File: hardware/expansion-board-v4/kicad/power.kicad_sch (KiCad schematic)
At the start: 37 parts, among them J9 MX1.25WT-2P BAT, U1 ME6211C33M5, U18 CH224K, U19 SY6970, U2 TPS7A2033PDBVR, U20 SY7069, U3 TPS7A2033PDBVR

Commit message: fix(hw): 103AT-2 是插件不是贴片，封装/焊盘/位置全部修正
## 主 bug：RT1 用错封装

103AT-2（SEMITEC 日本石塚）是**轴向引线玻璃封装的插件**，我之前直接套了
R_0603_1608Metric——焊盘、3D、装配全错，根因是没查 datasheet。

改为自建 NTC_103AT-2_Leaded_P2.54mm：两个 ⌀0.7 通孔、间距 2.54mm，
courtyard 只覆盖焊盘不含本体——因为 NTC 玻璃头不留在板面，靠引线延伸
平贴到电池表面。

位置从 (136.93,87.93) 改到 **(125.5,89.5)**，两个判据：
  · CHG_NTC 到分压电阻 R39/R40 只有 4.06mm。这是高阻模拟节点，
    原位置离分压网络 30mm，长走线会耦合开关噪声
  · 焊盘落在电池投影区内，玻璃头平贴板面与电池之间（电池仓净高 11.0
    − 电池 9.5 = 1.5mm 余量，刚好容下 ⌀1.5mm 玻璃头），热耦合最好

选点时扫描了两面 courtyard（通孔件会穿透）、螺丝孔让位圈、天线禁铺区。

## 连带修复：.kicad_mod 不能写 ';;' 注释

上一轮给 MX1.25WT-2P 封装加 3D 说明时用了 ';;'，那是 Lisp 语法，
KiCad 的 S-expression 解析器不认——**整个封装文件直接加载失败**，
而且不报错，只是 FootprintLoad 返回 None。逐个测试库中封装才发现
MX1.25WT-2P 和新建的 NTC 两个都是坏的。注释一律移进 (descr ...)。

## Python 环境：按 CLAUDE.md 用 ServBay

之前 gen_bom_smt.py 报缺 openpyxl，是因为我用了 KiCad 内置的 Python
（那个只该用于需要 pcbnew 的脚本）。ServBay 的 python3 3.13.12 本来就有
openpyxl 3.1.5。现在分工明确：
  · 需要 pcbnew 的（gen_assembly/gen_checklist）→ KiCad Python
  · 纯数据处理的（gen_bom/gen_bom_smt）→ ServBay Python

BOM_采购清单.xlsx（55 项）与 BOM_嘉立创SMT.xlsx（79 料号/162 贴片位）已补出。

## 新增待决项 D3：电源区电容建议 0603 → 0805

不是为了散热（电阻功率算过，R43 最大也才 32.5mW，0603 有 3 倍余量），
而是 DC bias 衰减和耐压可得性：**C72 要 6.8µF/25V，0603 根本买不到**
（0603 在 25V 档容值上限约 1~2.2µF），而它接 9V 侧耐压不能降。
换封装会动 B 面布局，等确认。

验收：原理图↔PCB 封装零不一致，DRC error 0 条，覆铜已重填。
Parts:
- RT1: footprint Resistor_SMD:R_0603_1608Metric -> expansion-board-v4:NTC_103AT-2_Leaded_P2.54mm
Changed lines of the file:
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@@
 			(effects (font (size 1.27 1.27)))
 		)
-		(property "Footprint" "Resistor_SMD:R_0603_1608Metric"
+		(property "Footprint" "expansion-board-v4:NTC_103AT-2_Leaded_P2.54mm"
 			(at 177.8 208.28 0)
 			(effects (font (size 1.27 1.27))

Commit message: fix(hw): NTC 改用贴片 NCP18XH103F03RB —— 电池是 3M 胶贴死的，插件放不下
## 为什么又改一次

上一轮把 RT1 从 R0603 改成插件封装，理由是「103AT-2 是轴向引线玻璃件」。
那步是对的，但方案错了：**电池用 3M 胶直接贴在 B 面**（防晃动脱落，同时给
背壳散热孔留空间），板面与电池之间**没有间隙**，玻璃头无处安放。
我上一版假设有 1.5mm 余量（11.0 电池仓 − 9.5 电池），那是"电池悬空"的算法，
与实际装配方式不符。

回到贴片，但换成真正的贴片 NTC 型号，不是拿普通电阻封装凑数：
NCP18XH103F03RB（Murata 0603 10k 1%）/ TDK NTCG163JF103FT1 / 国产 0603 10K 1%。

## NTC 本身不能删

SY6970 的 TS 是锂电池充电安全强制项：<0°C 充电析锂（枝晶刺穿隔膜、内短路），
>60°C 加速老化乃至热失控。不接就得用固定电阻假装永远 25°C，等于关掉保护。

座舱 80°C 的担心已查证：TS 保护**只作用于充电路径**。高温时停充，但
PMID→SYS 直供与 BAT→SYS 放电都不受限，设备照常运行，降温自动恢复。
去掉 NTC 才会在 80°C 继续充电，那才是不可预测的后果。

## B 值差异不需要改硬件

103AT-2 是 B25/85=3435K；Murata NCP18XH103 常标 B25/50=3380K，
但同一颗料在 B25/85 口径下是 3428K——差 0.2%，保护阈值偏移 <1°C，
分压电阻 R39/R40 保持不变。要抠精度改 MCU 侧查表/Steinhart-Hart 的 B 参数。

## 位置 (125.25, 88.00)

三个约束一起解出来的：在电池投影区内直接贴电池 / 距板上开关电源 ≥19mm
（否则测的是板温不是电池温）/ CHG_NTC 到分压电阻 R39/R40 仅 4.00mm
（高阻模拟节点，走线长了耦合开关噪声）。

已删除废弃的 NTC_103AT-2_Leaded_P2.54mm 封装，免得下次误用。

验收：DRC error 0 条，原理图↔PCB 一致，全套 BOM/装配文档重生成
（BOM 88 料号、SMT 79 料号 162 贴片位、ASSEMBLY 162 件、CHECKLIST 174 位号）。
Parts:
- RT1: value 103AT-2 10k NTC -> NCP18XH103F03RB 10k NTC; footprint expansion-board-v4:NTC_103AT-2_Leaded_P2.54mm -> Resistor_SMD:R_0603_1608Metric
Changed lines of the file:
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@@
 			(effects (font (size 1.27 1.27)))
 		)
-		(property "Value" "103AT-2 10k NTC"
+		(property "Value" "NCP18XH103F03RB 10k NTC"
 			(at 177.8 205.74 0)
 			(effects (font (size 1.27 1.27)))
 		)
-		(property "Footprint" "expansion-board-v4:NTC_103AT-2_Leaded_P2.54mm"
+		(property "Footprint" "Resistor_SMD:R_0603_1608Metric"
 			(at 177.8 208.28 0)
 			(effects (font (size 1.27 1.27))

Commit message: feat(hw): 实现「单面可用」——J4 移 F 面、补 CC 下拉、电源电容改封装
## 单面可用是保底

不带电源版的 B 面现在**零贴装件**，可以走嘉立创经济型单面（¥267.1），
不必被迫上标准型双面（¥614.96）。上一版把 J4 留在 B 面，等于不带电源版
还是双面，只省 ¥35，白做。

三个改动：

  J4 (USB-C) → F 面 (144.63,73.00) rot=0
      courtyard 右沿贴齐板边 150，开口仍朝 +X（与微雪 H1 同侧）。
      翻面会镜像 x 且 USB-C 封装原点不在几何中心，x 是重新解出来的。
      USB_DP/DM 连的 R9/R10 本来就在 F 面 x117，搬过去走线反而更短；
      USB_CC1/2 与 USB_VBUS 只有带电源版才用，跨面过孔即可。

  新增 R7/R8（5.1k CC 下拉）→ F 面，紧邻 J4 2.2mm
      不带电源版没有 CH224K，CC 悬空则主机根本不认设备——USB-C 规范要求
      device 端呈现 Rd 才会被检测和枚举，不枚举就没法 UF2 刷机。
      **与 CH224K 二选一**，带电源版不贴。

  R37 (138.80,69.84) → (137.75,70.75)
      J4 的通孔安装脚穿到 B 面，落进了 R37 的 courtyard（DRC 报
      pth_inside_courtyard）。顺带把它到 CH224K CFG1 脚的距离 2.97→2.56mm。

## 电源电容改封装

不是为散热——电阻功率算过，最大的 R43 也才 (9−3.3)²/1k = 32.5mW，
0603 有 3 倍余量。真正的理由是两条：

  C72  6.8µF/25V  0603 → 1206
      接 PD 诱骗后的 9V 侧，耐压不能降。而 0603 在 25V 档容值上限只有
      1~2.2µF，6.8µF/25V 根本买不到。换封装后原位撞 C80，已就近重贴
      （按「离同网芯片引脚最近」而不是「离原位最近」找的位）。

  C73/C74/C75  10µF  0603 → 0805
      直流偏置下的容值衰减：10µF/16V X5R 在 5V 偏压下，0603 只剩
      3~4µF(−60%)，0805 还有 6~7µF(−30%)，直接影响输出纹波。

## 新增电源采购 CSV（单独一份，不混进整板 xlsx）

tools/gen_power_csv.py → BOM_电源采购_淘宝.csv，22 种料 / 30 颗。
按「卖家怎么找货」分组，同规格合并给总数，备注写清耐压/精度/为什么
封装不能换，末尾附两个版本的贴装差异。整板 88 料号的 xlsx 发给卖家太乱。

验收：DRC error 0 条，F 面丝印全通过，原理图↔PCB 零不一致，
176 元件已固化，全套文档重生成（BOM 88 料号 / SMT 79 料号 164 贴片位）。
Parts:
- C72: footprint Capacitor_SMD:C_0603_1608Metric -> Capacitor_SMD:C_1206_3216Metric
- C73, C74, C75: footprint Capacitor_SMD:C_0603_1608Metric -> Capacitor_SMD:C_0805_2012Metric
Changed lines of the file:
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@@
 			(effects (font (size 1.27 1.27)))
 		)
-		(property "Footprint" "Capacitor_SMD:C_0603_1608Metric"
+		(property "Footprint" "Capacitor_SMD:C_1206_3216Metric"
 			(at 177.8 144.78 0)
 			(effects (font (size 1.27 1.27))
@@
 			(effects (font (size 1.27 1.27)))
 		)
-		(property "Footprint" "Capacitor_SMD:C_0603_1608Metric"
+		(property "Footprint" "Capacitor_SMD:C_0805_2012Metric"
 			(at 203.2 182.88 0)
 			(effects (font (size 1.27 1.27))
@@
 			(effects (font (size 1.27 1.27)))
 		)
-		(property "Footprint" "Capacitor_SMD:C_0603_1608Metric"
+		(property "Footprint" "Capacitor_SMD:C_0805_2012Metric"
 			(at 215.9 182.88 0)
 			(effects (font (size 1.27 1.27))
@@
 			(effects (font (size 1.27 1.27)))
 		)
-		(property "Footprint" "Capacitor_SMD:C_0603_1608Metric"
+		(property "Footprint" "Capacitor_SMD:C_0805_2012Metric"
 			(at 203.2 195.58 0)
 			(effects (font (size 1.27 1.27))

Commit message: fix(v4): correct RF and power networks for V4.2
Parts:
- C72: value 6.8uF -> 10uF
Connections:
- net USB_CC1: now also U18.7 (CC2); no longer U18.6 (CC1)
- net USB_CC2: now also U18.6 (CC1); no longer U18.7 (CC2)
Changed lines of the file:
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@@
+		(effects (font (size 1.27 1.27)) (justify left))
+	)
+	(global_label "USB_CC2"
+		(shape passive)
+		(at 93.98 162.56 0)
 		(effects (font (size 1.27 1.27)) (justify left))
 	)
 	(global_label "USB_CC1"
-		(shape passive)
-		(at 93.98 162.56 0)
-		(effects (font (size 1.27 1.27)) (justify left))
-	)
-	(global_label "USB_CC2"
 		(shape passive)
 		(at 93.98 165.1 0)
@@
 			(effects (font (size 1.27 1.27)))
 		)
-		(property "Value" "6.8uF"
+		(property "Value" "10uF"
 			(at 177.8 142.24 0)
 			(effects (font (size 1.27 1.27)))

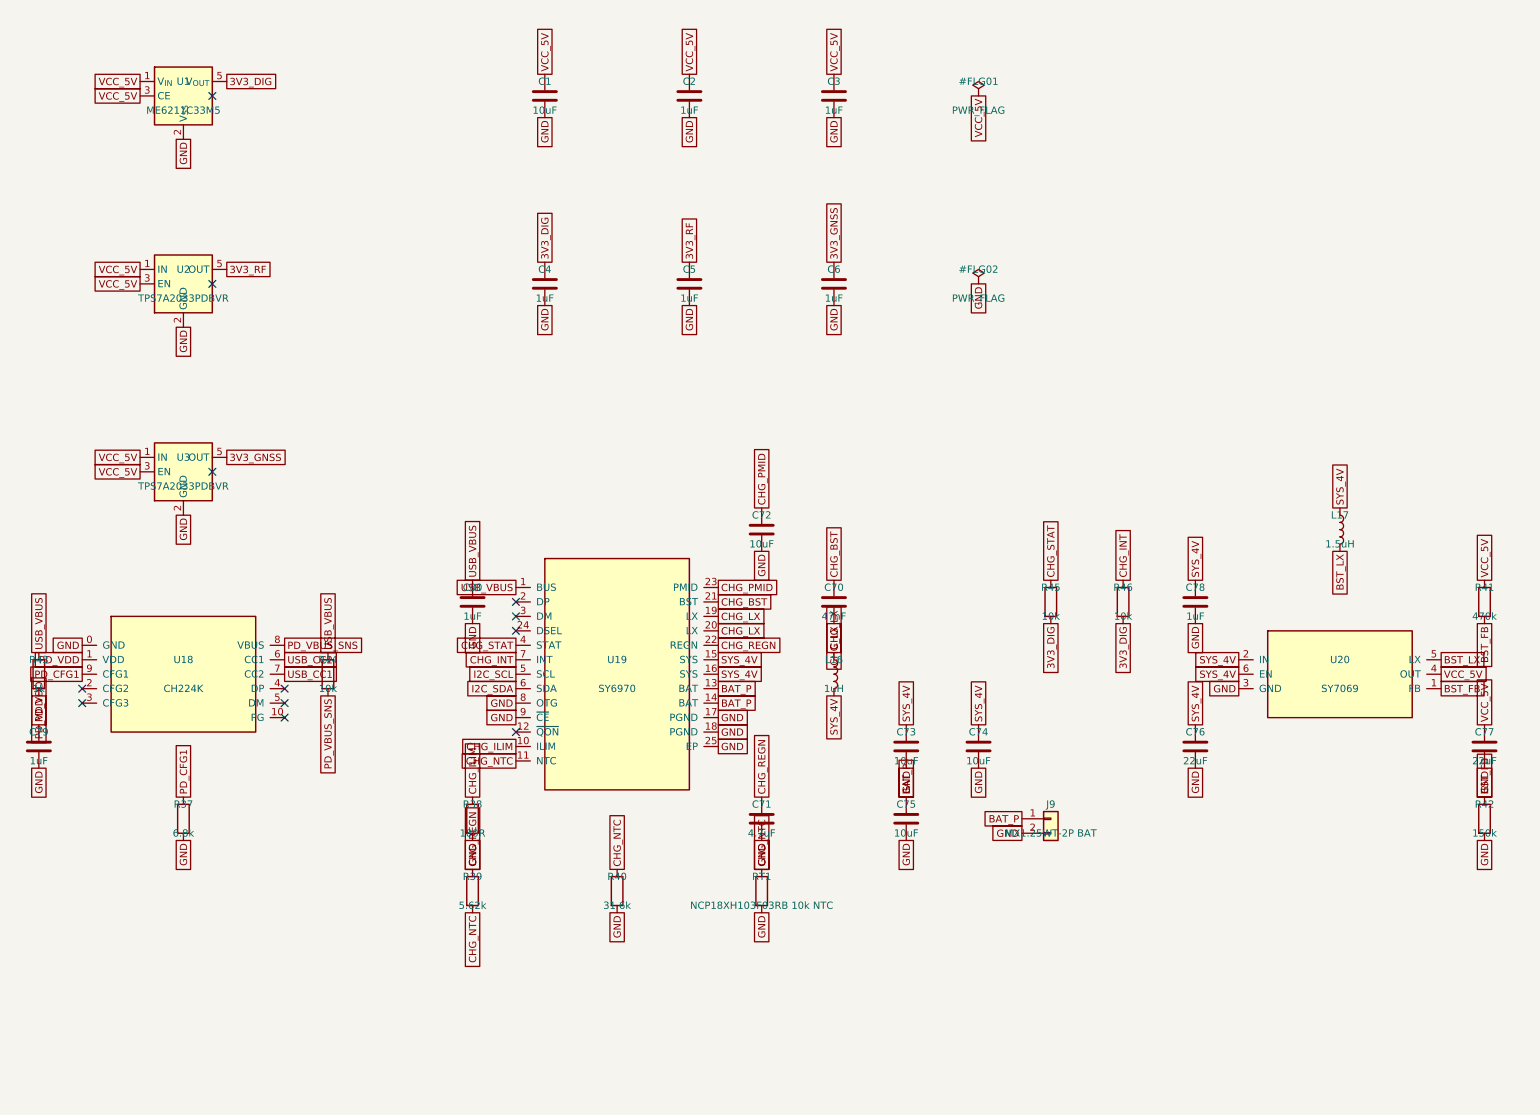
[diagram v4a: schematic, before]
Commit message: fix(v4): finalize V4.3 board after manual routing
罩哥手工完成全部布线后的定稿。DRC 0 violations / 0 unconnected。

板子本身:
- 1607 段走线 / 415 个过孔 / 207 个封装 / 15 个 zone
- RP_1V1 在 B.Cu 合并为单块 228.96mm2，四颗 RP_1V1 去耦落入其中
- C81 挪到 U12 旁 1.47mm(原 3.36mm)，脚下由「无铜」变为落在 B.Cu 的 3V3_RF 上
- U8.23(DVDD) 补一个 RP_1V1 过孔 @(85.798,72.600)，接入距离 1.63 -> 0.88mm
  落点在既有走线上，未改任何走线；与相邻 QFN 焊盘边缘间距 +0.312mm

原理图:
- rf1090 的 PWR_FLAG 由 #FLG05 改为 #FLG06。sheet_power.py 已占用 #FLG05,
  两页撞号会让网表导出报「批注错误」。改后网表 714 节点、网络归属零变化。

.kicad_pro 保留正式板原有的 FINE netclass(0.13mm, 用于 DEMOD0-3/RECOVERED_CLK/
SWCLK/SWDIO)。板上这 7 个网络实际都按 0.15mm 布线、FINE 处于闲置; 两份工程
文件下各跑一次 DRC 均为 0，且 drc_exclusions 都是空的。
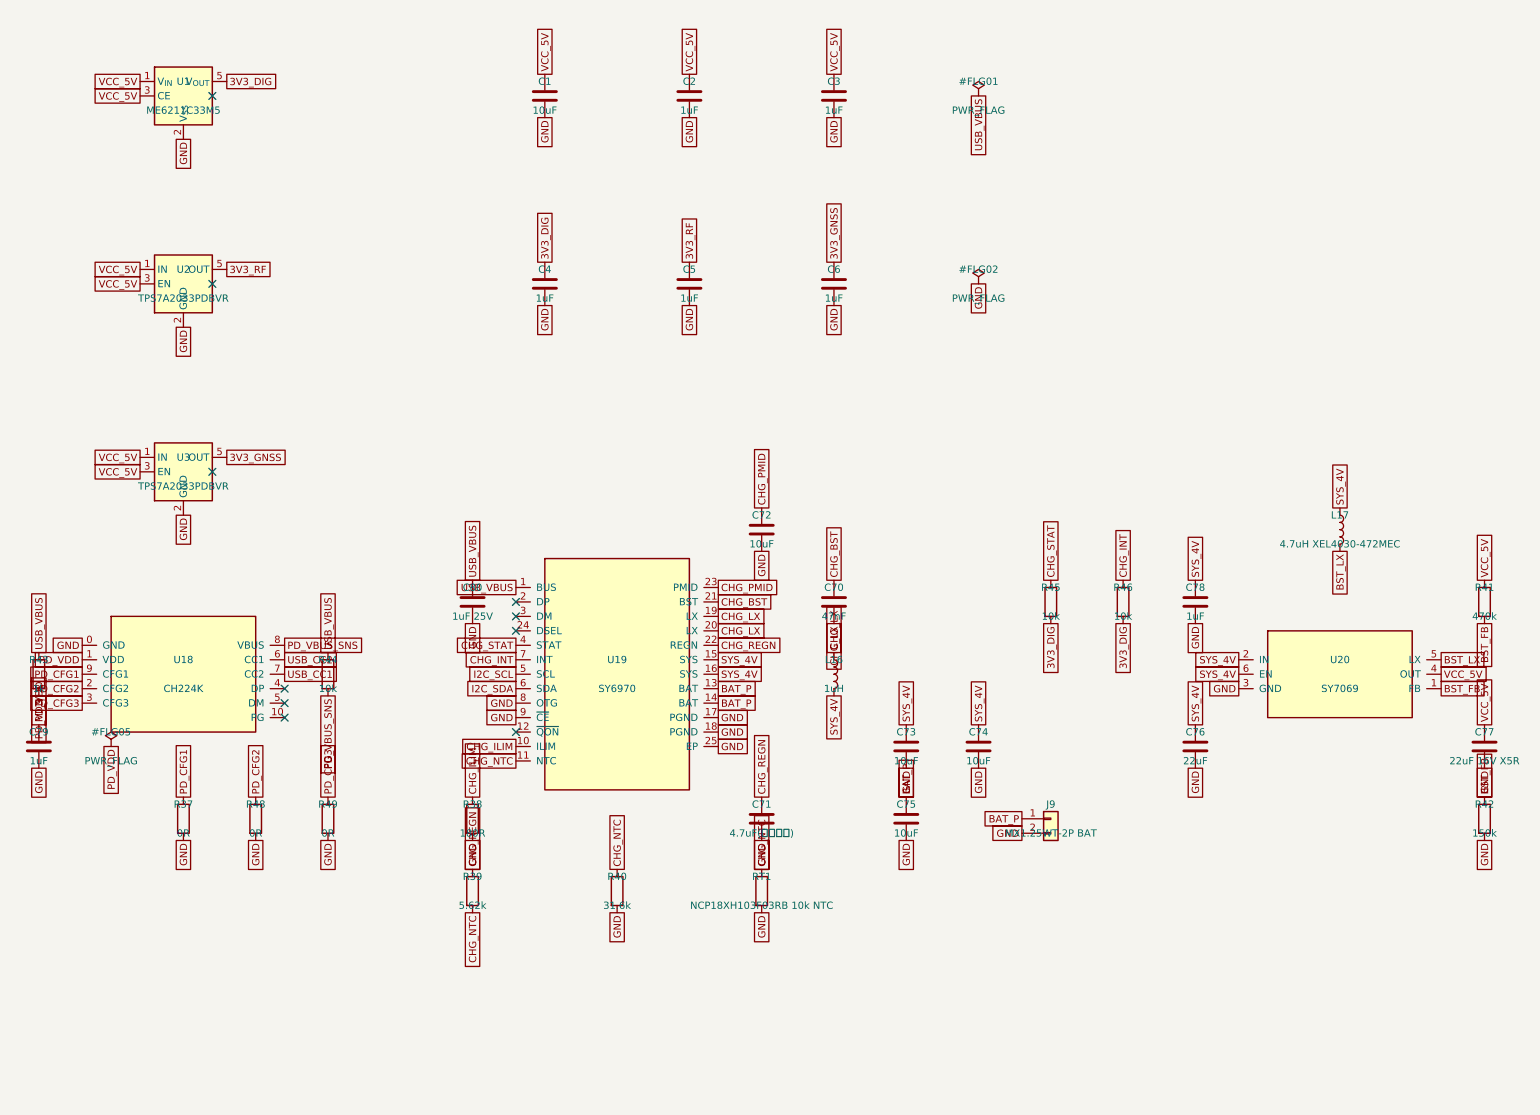
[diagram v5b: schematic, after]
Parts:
- added R48, R49: 0R, Resistor_SMD:R_0603_1608Metric, symbol Device:R
- C71: value 4.7uF -> 4.7uF(带电源版)
- C77: value 22uF -> 22uF 16V X5R
- C80: value 1uF -> 1uF 25V
- L17: value 1.5uH -> 4.7uH XEL4030-472MEC; footprint Inductor_SMD:L_Bourns-SRN4018 -> Inductor_SMD:L_Coilcraft_XxL4030
- R37: value 6.8k -> 0R
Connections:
- net GND: now also R48.2, R49.2
- net PD_CFG2: now reaches U18.2 (CFG2)
- net PD_CFG2: now also R48.1
- net PD_CFG3: now reaches U18.3 (CFG3)
- net PD_CFG3: now also R49.1
- no-connect marks 12 -> 10
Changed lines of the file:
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@@
 		)
 	)
-	(global_label "VCC_5V"
+	(global_label "USB_VBUS"
 		(shape passive)
 		(at 215.9 63.5 90)
@@
 		(pin "1"
 		)
+		(pin "9"
+		)
 		(pin "2"
 		)
 		(pin "3"
 		)
+		(pin "8"
+		)
+		(pin "6"
+		)
+		(pin "7"
+		)
 		(pin "4"
 		)
 		(pin "5"
 		)
-		(pin "6"
-		)
-		(pin "7"
-		)
-		(pin "8"
-		)
-		(pin "9"
-		)
 		(pin "10"
 		)
@@
 		(effects (font (size 1.27 1.27)) (justify right))
 	)
-	(no_connect
-		(at 58.42 167.64)
-	)
-	(no_connect
-		(at 58.42 170.18)
+	(global_label "PD_CFG2"
+		(shape passive)
+		(at 58.42 167.64 180)
+		(effects (font (size 1.27 1.27)) (justify right))
+	)
+	(global_label "PD_CFG3"
+		(shape passive)
+		(at 58.42 170.18 180)
+		(effects (font (size 1.27 1.27)) (justify right))
 	)
 	(global_label "PD_VBUS_SNS"
@@
 	)
 	(symbol
+		(lib_id "power:PWR_FLAG")
+		(at 63.5 177.8 0)
+		(unit 1)
+		(exclude_from_sim no)
+		(in_bom yes)
+		(on_board yes)
+		(dnp no)
+		(property "Reference" "#FLG05"
+			(at 63.5 175.26 0)
+			(effects (font (size 1.27 1.27)))
+		)
+		(property "Value" "PWR_FLAG"
+			(at 63.5 180.34 0)
+			(effects (font (size 1.27 1.27)))
+		)
+		(property "Footprint" ""
+			(at 63.5 182.88 0)
+			(effects (font (size 1.27 1.27))
+				(hide yes))
+		)
+		(property "Datasheet" "~"
+			(at 63.5 185.42 0)
+			(effects (font (size 1.27 1.27))
+				(hide yes))
+		)
+		(pin "1"
+		)
+		(instances
+			(project "expansion-board-v4"
+				(path "/10000000-0000-4000-8000-000000000001/20000000-0000-4000-8000-000000000001"
+					(reference "#FLG05")
+					(unit 1)
+				)
+			)
+		)
+	)
+	(global_label "PD_VDD"
+		(shape passive)
+		(at 63.5 177.8 90)
+		(effects (font (size 1.27 1.27)) (justify right))
+	)
+	(symbol
 		(lib_id "Device:R")
 		(at 101.6 165.1 0)
@@
 			(effects (font (size 1.27 1.27)))
 		)
-		(property "Value" "6.8k"
+		(property "Value" "0R"
 			(at 76.2 193.04 0)
 			(effects (font (size 1.27 1.27)))
@@
 	)
 	(symbol
+		(lib_id "Device:R")
+		(at 88.9 190.5 0)
+		(unit 1)
+		(exclude_from_sim no)
+		(in_bom yes)
+		(on_board yes)
+		(dnp no)
+		(property "Reference" "R48"
+			(at 88.9 187.96 0)
+			(effects (font (size 1.27 1.27)))
+		)
+		(property "Value" "0R"
+			(at 88.9 193.04 0)
+			(effects (font (size 1.27 1.27)))
+		)
+		(property "Footprint" "Resistor_SMD:R_0603_1608Metric"
+			(at 88.9 195.58 0)
+			(effects (font (size 1.27 1.27))
+				(hide yes))
+		)
+		(property "Datasheet" "~"
+			(at 88.9 198.12 0)
+			(effects (font (size 1.27 1.27))
+				(hide yes))
+		)
+		(pin "1"
+		)
+		(pin "2"
+		)
+		(instances
+			(project "expansion-board-v4"
+				(path "/10000000-0000-4000-8000-000000000001/20000000-0000-4000-8000-000000000001"
+					(reference "R48")
+					(unit 1)
+				)
+			)
+		)
+	)
+	(global_label "PD_CFG2"
+		(shape passive)
+		(at 88.9 186.69 270)
+		(effects (font (size 1.27 1.27)) (justify left))
+	)
+	(global_label "GND"
+		(shape passive)
+		(at 88.9 194.31 90)
+		(effects (font (size 1.27 1.27)) (justify right))
+	)
+	(symbol
+		(lib_id "Device:R")
+		(at 101.6 190.5 0)
+		(unit 1)
+		(exclude_from_sim no)
+		(in_bom yes)
+		(on_board yes)
+		(dnp no)
+		(property "Reference" "R49"
+			(at 101.6 187.96 0)
+			(effects (font (size 1.27 1.27)))
+		)
+		(property "Value" "0R"
+			(at 101.6 193.04 0)
+			(effects (font (size 1.27 1.27)))
+		)
+		(property "Footprint" "Resistor_SMD:R_0603_1608Metric"
+			(at 101.6 195.58 0)
+			(effects (font (size 1.27 1.27))
+				(hide yes))
+		)
+		(property "Datasheet" "~"
+			(at 101.6 198.12 0)
+			(effects (font (size 1.27 1.27))
+				(hide yes))
+		)
+		(pin "1"
+		)
+		(pin "2"
+		)
+		(instances
+			(project "expansion-board-v4"
+				(path "/10000000-0000-4000-8000-000000000001/20000000-0000-4000-8000-000000000001"
+					(reference "R49")
+					(unit 1)
+				)
+			)
+		)
+	)
+	(global_label "PD_CFG3"
+		(shape passive)
+		(at 101.6 186.69 270)
+		(effects (font (size 1.27 1.27)) (justify left))
+	)
+	(global_label "GND"
+		(shape passive)
+		(at 101.6 194.31 90)
+		(effects (font (size 1.27 1.27)) (justify right))
+	)
+	(symbol
 		(lib_id "expansion-board-v4:SY6970")
 		(at 152.4 165.1 0)
@@
 		(pin "3"
 		)
+		(pin "24"
+		)
 		(pin "4"
 		)
+		(pin "7"
+		)
 		(pin "5"
 		)
 		(pin "6"
 		)
-		(pin "7"
-		)
 		(pin "8"
 		)
 		(pin "9"
 		)
+		(pin "12"
+		)
 		(pin "10"
 		)
 		(pin "11"
 		)
-		(pin "12"
+		(pin "23"
+		)
+		(pin "21"
+		)
+		(pin "19"
+		)
+		(pin "20"
+		)
+		(pin "22"
+		)
+		(pin "15"
+		)
+		(pin "16"
 		)
 		(pin "13"
@@
 		(pin "14"
 		)
-		(pin "15"
-		)
-		(pin "16"
-		)
 		(pin "17"
 		)
 		(pin "18"
-		)
-		(pin "19"
-		)
-		(pin "20"
-		)
-		(pin "21"
-		)
-		(pin "22"
-		)
-		(pin "23"
-		)
-		(pin "24"
 		)
 		(pin "25"
@@
 			(effects (font (size 1.27 1.27)))
 		)
-		(property "Value" "1uF"
+		(property "Value" "1uF 25V"
 			(at 127 154.94 0)
 			(effects (font (size 1.27 1.27)))
@@
 			(effects (font (size 1.27 1.27)))
 		)
-		(property "Value" "4.7uF"
+		(property "Value" "4.7uF(带电源版)"
 			(at 177.8 193.04 0)
 			(effects (font (size 1.27 1.27)))
@@
 				(hide yes))
 		)
-		(pin "1"
-		)
-		(pin "2"
+		(pin "2"
+		)
+		(pin "6"
 		)
 		(pin "3"
 		)
+		(pin "5"
+		)
 		(pin "4"
 		)
-		(pin "5"
-		)
-		(pin "6"
+		(pin "1"
 		)
 		(instances
@@
 			(effects (font (size 1.27 1.27)))
 		)
-		(property "Value" "1.5uH"
+		(property "Value" "4.7uH XEL4030-472MEC"
 			(at 279.4 142.24 0)
 			(effects (font (size 1.27 1.27)))
 		)
-		(property "Footprint" "Inductor_SMD:L_Bourns-SRN4018"
+		(property "Footprint" "Inductor_SMD:L_Coilcraft_XxL4030"
 			(at 279.4 144.78 0)
 			(effects (font (size 1.27 1.27))
@@
 			(effects (font (size 1.27 1.27)))
 		)
-		(property "Value" "22uF"
+		(property "Value" "22uF 16V X5R"
 			(at 304.8 180.34 0)
 			(effects (font (size 1.27 1.27)))

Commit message: fix(v4): correct stale SMT placement files and lock IOVDD locality
Two of the three CPL variants still carried the pre-migration coordinates
for C22-C27 and shipped that way in 543c346. gen_jlc_smt.py takes the
variant as an argument and only regenerates `passives` when called bare,
so re-running it once after moving the decouplers left `minimal` and
`passives` pointing at footprint positions that no longer exist:

    C22  121.25 -> 93.218      C25  124.40 -> 83.250
    C23  124.40 -> 91.800      C26  121.25 -> 78.927
    C24  121.25 -> 80.927      C27  124.40 -> 77.900

Designator sets, row counts and DNP filtering were all correct in the
stale files, which is why the earlier "BOM/CPL designators match" check
passed over it. All three variants are now regenerated and a contract
assertion compares every CPL row against the board's own placement
(Mid X = centre x, Mid Y = -centre y), so a missed variant fails loudly.

Also lock the decoupler locality that 543c346 established. The existing
plane-reachability assertions say nothing about position - the 30 mm
layout satisfied them just as well. The new check runs in both
directions per power net: every U8 power pin must have a nearby cap, and
every cap must sit near a pin. Candidate pools are grouped by net rather
than by the reviewer's list: C82/C83 sit on RP_1V1 6.10/7.65 mm from U8
and are part of the local set, not exemptions - only C84/C85/C86 are
genuinely remote. Calibrated against counter-examples in a sandbox copy:
C27 pushed 1.0 mm outward still passes, 1.5 mm trips; restoring the old
layout trips 15 assertions. It does not catch stacking (six caps piled on
U8's centre passes) - DRC courtyard overlap covers that, and the comment
says so.

Sync U19's schematic footprint to the in-project library so it agrees
with the PCB, restoring schematic parity from 23 to 22. Fixed in
sheet_power.py, not the generated file - a full rebuild reproduces all
seven schematics byte-for-byte.

Refresh the board scale in README an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
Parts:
- U19: footprint Package_DFN_QFN:QFN-24-1EP_4x4mm_P0.5mm_EP2.6x2.6mm_ThermalVias -> expansion-board-v4:QFN-24-1EP_4x4mm_P0.5mm_EP2.6x2.6mm_ThermalVias
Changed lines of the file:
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@@
 			(effects (font (size 1.27 1.27)))
 		)
-		(property "Footprint" "Package_DFN_QFN:QFN-24-1EP_4x4mm_P0.5mm_EP2.6x2.6mm_ThermalVias"
+		(property "Footprint" "expansion-board-v4:QFN-24-1EP_4x4mm_P0.5mm_EP2.6x2.6mm_ThermalVias"
 			(at 152.4 170.18 0)
 			(effects (font (size 1.27 1.27))
